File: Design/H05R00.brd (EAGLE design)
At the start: 60 x 34.6 mm, 59 parts, among them Q1 ECH8693R-TL-W, U1 STM32G0B1CEU6N, U2 MAX17330X22+, U3 TPS631000DRLR, U4 LD39200PU33R, X1 XTALL_CSTCE8M00G52

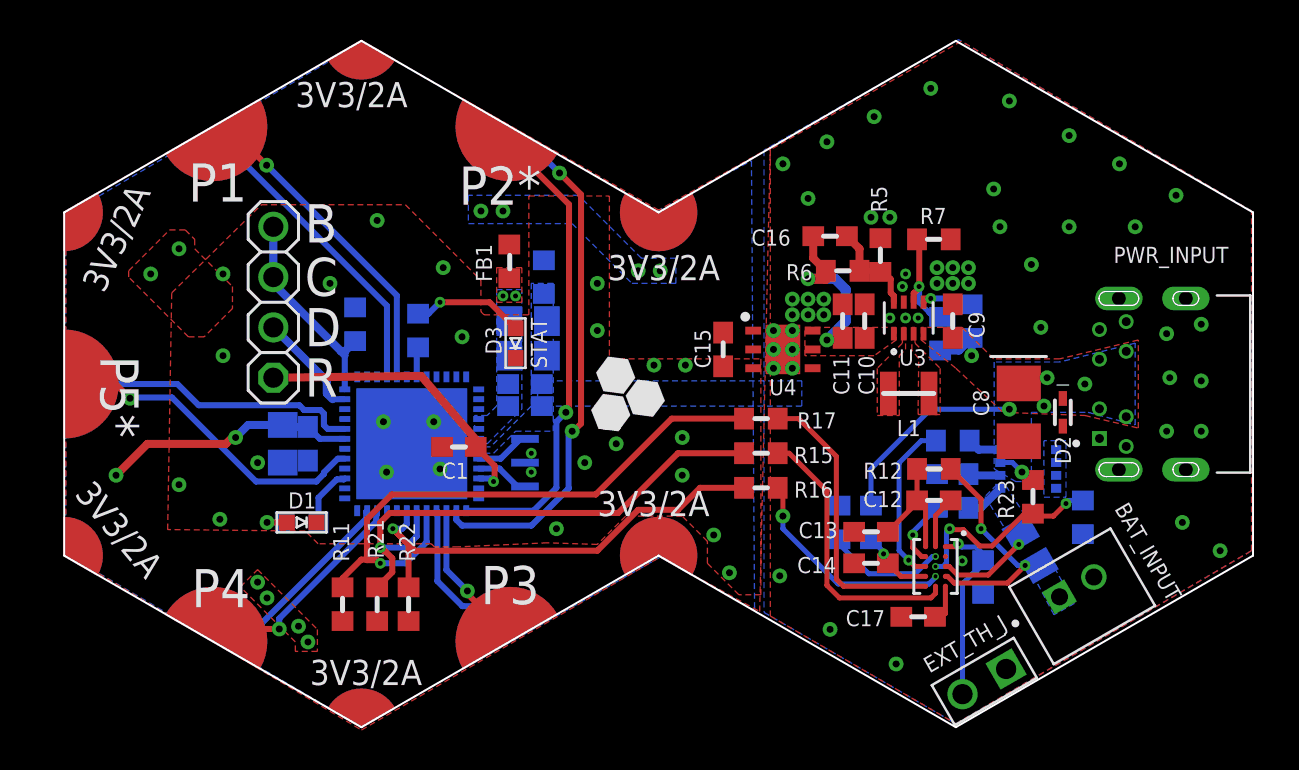
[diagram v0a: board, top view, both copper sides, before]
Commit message: - Add power pads for the power hexagon and improve the silkscreen layer look
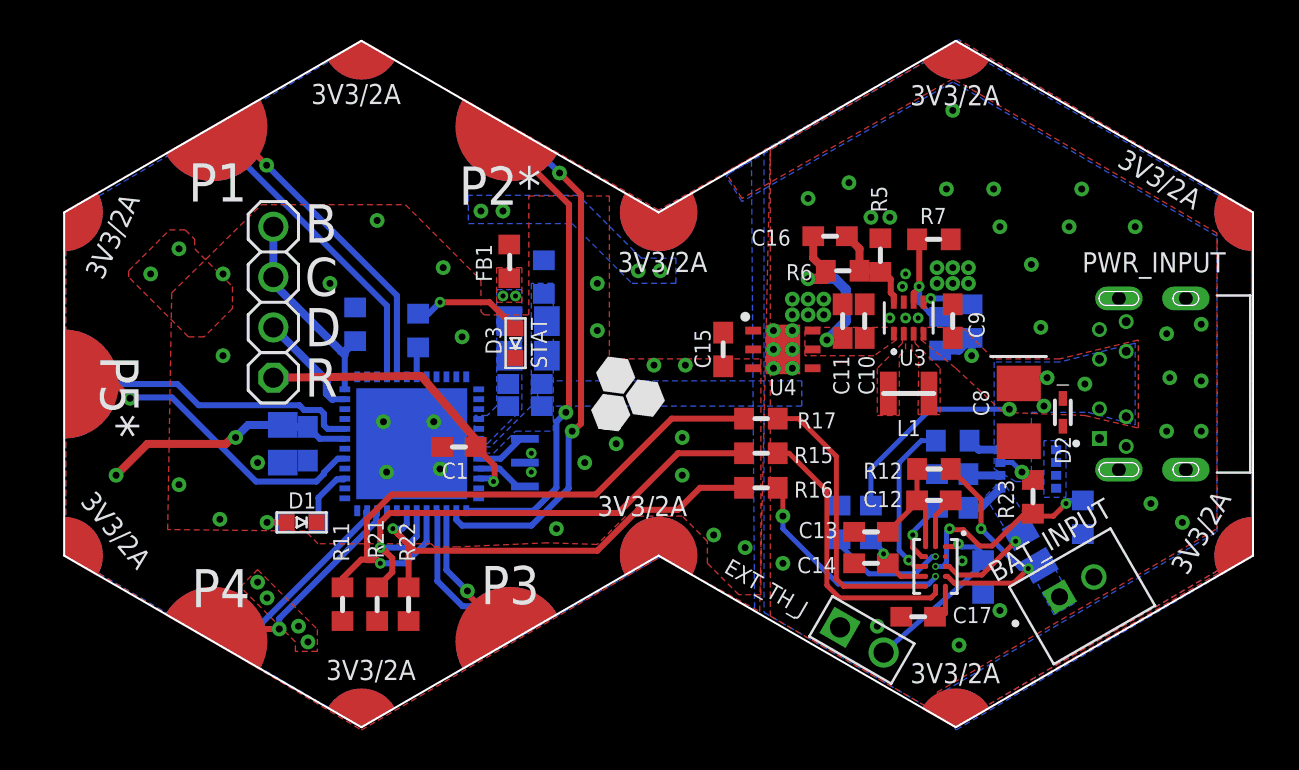
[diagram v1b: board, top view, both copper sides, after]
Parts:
- U$1: value HEXABIT_X2_P1_P5_NO_POWER_PADS -> HEXABIT_X2_P1_P5; device hexabitz_connectors:HEXABIT_X2_P1_P5_NO_POWER_PADS -> hexabitz_connectors:HEXABIT_17.32_X2_P1_P5
- moved EXT_TH_J 8.64 mm to (9.23, -3.55), turned to 330 degrees
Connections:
- net GND: now also U$1.PAD_PD14, U$1.PAD_PD15, U$1.PAD_PD16, U$1.PAD_PD17
- net VDD: now also U$1.PAD_PU14, U$1.PAD_PU15, U$1.PAD_PU16, U$1.PAD_PU17
